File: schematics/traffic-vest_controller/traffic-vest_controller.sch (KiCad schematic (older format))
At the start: 21 parts

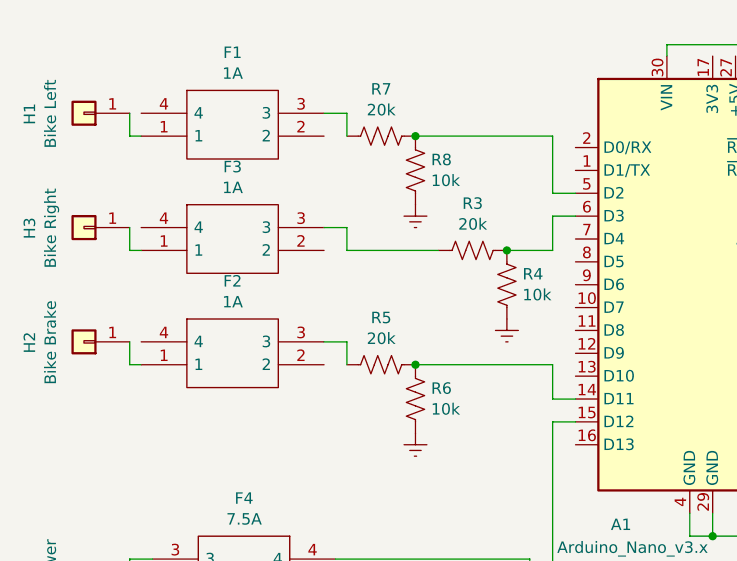
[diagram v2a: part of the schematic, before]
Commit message: Flipped nano, rearranged digital pin connecctions, futzed with connection spacing, re-routed tracks
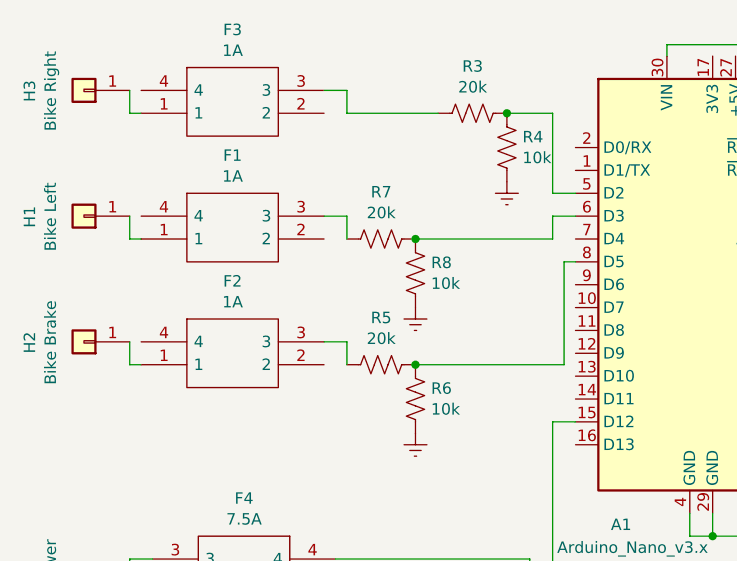
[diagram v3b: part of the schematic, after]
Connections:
- net at R5.1, R6.1: now also A1.8 (D5); no longer A1.14 (D11)
- net at R7.1, R8.1: now also A1.6 (D3); no longer A1.5 (D2)
- net at R3.1, R4.1: now also A1.5 (D2); no longer A1.6 (D3)
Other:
- moved on the sheet: F1, F3, H1, H3, R3, R4, R7, R8
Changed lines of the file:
@@
 L power:GNDREF #PWR0107
 U 1 1 62145970
-P 5400 3050
-F 0 "#PWR0107" H 5400 2800 50  0001 C CNN
-F 1 "GNDREF" H 5405 2877 50  0001 C CNN
-F 2 "" H 5400 3050 50  0001 C CNN
-F 3 "" H 5400 3050 50  0001 C CNN
-	1    5400 3050
+P 5400 2450
+F 0 "#PWR0107" H 5400 2200 50  0001 C CNN
+F 1 "GNDREF" H 5405 2277 50  0001 C CNN
+F 2 "" H 5400 2450 50  0001 C CNN
+F 3 "" H 5400 2450 50  0001 C CNN
+	1    5400 2450
 	1    0    0    -1
 $EndComp
@@
 L Device:R_US R3
 U 1 1 620FD795
-P 5250 2750
-F 0 "R3" V 5045 2750 50  0000 C CNN
-F 1 "20k" V 5136 2750 50  0000 C CNN
-F 2 "Resistor_THT:R_Axial_DIN0204_L3.6mm_D1.6mm_P5.08mm_Horizontal" V 5290 2740 50  0001 C CNN
-F 3 "~" H 5250 2750 50  0001 C CNN
-	1    5250 2750
+P 5250 2150
+F 0 "R3" V 5045 2150 50  0000 C CNN
+F 1 "20k" V 5136 2150 50  0000 C CNN
+F 2 "Resistor_THT:R_Axial_DIN0204_L3.6mm_D1.6mm_P5.08mm_Horizontal" V 5290 2140 50  0001 C CNN
+F 3 "~" H 5250 2150 50  0001 C CNN
+	1    5250 2150
 	0    1    1    0
 $EndComp
@@
 L Device:R_US R4
 U 1 1 620FBD59
-P 5400 2900
-F 0 "R4" H 5468 2946 50  0000 L CNN
-F 1 "10k" H 5468 2855 50  0000 L CNN
-F 2 "Resistor_THT:R_Axial_DIN0204_L3.6mm_D1.6mm_P5.08mm_Horizontal" V 5440 2890 50  0001 C CNN
-F 3 "~" H 5400 2900 50  0001 C CNN
-	1    5400 2900
+P 5400 2300
+F 0 "R4" H 5468 2346 50  0000 L CNN
+F 1 "10k" H 5468 2255 50  0000 L CNN
+F 2 "Resistor_THT:R_Axial_DIN0204_L3.6mm_D1.6mm_P5.08mm_Horizontal" V 5440 2290 50  0001 C CNN
+F 3 "~" H 5400 2300 50  0001 C CNN
+	1    5400 2300
 	1    0    0    -1
 $EndComp
@@
 L power:GNDREF #PWR0108
 U 1 1 62143F63
-P 5000 2550
-F 0 "#PWR0108" H 5000 2300 50  0001 C CNN
-F 1 "GNDREF" H 5005 2377 50  0001 C CNN
-F 2 "" H 5000 2550 50  0001 C CNN
-F 3 "" H 5000 2550 50  0001 C CNN
-	1    5000 2550
+P 5000 3000
+F 0 "#PWR0108" H 5000 2750 50  0001 C CNN
+F 1 "GNDREF" H 5005 2827 50  0001 C CNN
+F 2 "" H 5000 3000 50  0001 C CNN
+F 3 "" H 5000 3000 50  0001 C CNN
+	1    5000 3000
 	1    0    0    -1
 $EndComp
@@
 L Device:R_US R7
 U 1 1 620FC6E1
-P 4850 2250
-F 0 "R7" V 4645 2250 50  0000 C CNN
-F 1 "20k" V 4736 2250 50  0000 C CNN
-F 2 "Resistor_THT:R_Axial_DIN0204_L3.6mm_D1.6mm_P5.08mm_Horizontal" V 4890 2240 50  0001 C CNN
-F 3 "~" H 4850 2250 50  0001 C CNN
-	1    4850 2250
+P 4850 2700
+F 0 "R7" V 4645 2700 50  0000 C CNN
+F 1 "20k" V 4736 2700 50  0000 C CNN
+F 2 "Resistor_THT:R_Axial_DIN0204_L3.6mm_D1.6mm_P5.08mm_Horizontal" V 4890 2690 50  0001 C CNN
+F 3 "~" H 4850 2700 50  0001 C CNN
+	1    4850 2700
 	0    1    1    0
 $EndComp
@@
 L Device:R_US R8
 U 1 1 620FA2CA
-P 5000 2400
-F 0 "R8" H 5068 2446 50  0000 L CNN
-F 1 "10k" H 5068 2355 50  0000 L CNN
-F 2 "Resistor_THT:R_Axial_DIN0204_L3.6mm_D1.6mm_P5.08mm_Horizontal" V 5040 2390 50  0001 C CNN
-F 3 "~" H 5000 2400 50  0001 C CNN
-	1    5000 2400
-	1    0    0    -1
-$EndComp
-Wire Wire Line
-	5600 2500 5700 2500
-Connection ~ 5000 2250
+P 5000 2850
+F 0 "R8" H 5068 2896 50  0000 L CNN
+F 1 "10k" H 5068 2805 50  0000 L CNN
+F 2 "Resistor_THT:R_Axial_DIN0204_L3.6mm_D1.6mm_P5.08mm_Horizontal" V 5040 2840 50  0001 C CNN
+F 3 "~" H 5000 2850 50  0001 C CNN
+	1    5000 2850
+	1    0    0    -1
+$EndComp
+Connection ~ 5000 2700
 $Comp
 L Device:R_US R1
@@
 L traffic-vest_controller-rescue:3549-2-3549-2 F3
 U 1 1 622880EB
-P 3800 2650
-F 0 "F3" H 4200 2915 50  0000 C CNN
-F 1 "1A" H 4200 2824 50  0000 C CNN
-F 2 "3549-2:35492" H 4450 2750 50  0001 L CNN
-F 3 "https://componentsearchengine.com/Datasheets/1/3549-2.pdf" H 4450 2650 50  0001 L CNN
-F 4 "Fuse Holder FUSE SOCKET MINI HORZ .700 X .394" H 4450 2550 50  0001 L CNN "Description"
-F 5 "5.66" H 4450 2450 50  0001 L CNN "Height"
-F 6 "534-3549-2" H 4450 2350 50  0001 L CNN "Mouser Part Number"
-F 7 "https://www.mouser.co.uk/ProductDetail/Keystone-Electronics/3549-2?qs=fP5bVVCrK%2Fei3gwwxH1JKw%3D%3D" H 4450 2250 50  0001 L CNN "Mouser Price/Stock"
-F 8 "Keystone Electronics" H 4450 2150 50  0001 L CNN "Manufacturer_Name"
-F 9 "3549-2" H 4450 2050 50  0001 L CNN "Manufacturer_Part_Number"
-	1    3800 2650
+P 3800 2050
+F 0 "F3" H 4200 2315 50  0000 C CNN
+F 1 "1A" H 4200 2224 50  0000 C CNN
+F 2 "3549-2:35492" H 4450 2150 50  0001 L CNN
+F 3 "https://componentsearchengine.com/Datasheets/1/3549-2.pdf" H 4450 2050 50  0001 L CNN
+F 4 "Fuse Holder FUSE SOCKET MINI HORZ .700 X .394" H 4450 1950 50  0001 L CNN "Description"
+F 5 "5.66" H 4450 1850 50  0001 L CNN "Height"
+F 6 "534-3549-2" H 4450 1750 50  0001 L CNN "Mouser Part Number"
+F 7 "https://www.mouser.co.uk/ProductDetail/Keystone-Electronics/3549-2?qs=fP5bVVCrK%2Fei3gwwxH1JKw%3D%3D" H 4450 1650 50  0001 L CNN "Mouser Price/Stock"
+F 8 "Keystone Electronics" H 4450 1550 50  0001 L CNN "Manufacturer_Name"
+F 9 "3549-2" H 4450 1450 50  0001 L CNN "Manufacturer_Part_Number"
+	1    3800 2050
 	1    0    0    -1
 $EndComp
@@
 L Connector_Generic:Conn_01x01 H1
 U 1 1 622B1C15
-P 3550 2150
-F 0 "H1" V 3787 2153 50  0000 C CNN
-F 1 "Bike Left" V 3696 2153 50  0000 C CNN
-F 2 "Connector_Wire:SolderWirePad_1x01_Drill1.5mm" H 3550 2150 50  0001 C CNN
-F 3 "~" H 3550 2150 50  0001 C CNN
-	1    3550 2150
+P 3550 2600
+F 0 "H1" V 3787 2603 50  0000 C CNN
+F 1 "Bike Left" V 3696 2603 50  0000 C CNN
+F 2 "Connector_Wire:SolderWirePad_1x01_Drill1.5mm" H 3550 2600 50  0001 C CNN
+F 3 "~" H 3550 2600 50  0001 C CNN
+	1    3550 2600
 	-1   0    0    1
 $EndComp
@@
 L Connector_Generic:Conn_01x01 H3
 U 1 1 622B1527
-P 3550 2650
-F 0 "H3" V 3787 2653 50  0000 C CNN
-F 1 "Bike Right" V 3696 2653 50  0000 C CNN
-F 2 "Connector_Wire:SolderWirePad_1x01_Drill1.5mm" H 3550 2650 50  0001 C CNN
-F 3 "~" H 3550 2650 50  0001 C CNN
-	1    3550 2650
+P 3550 2050
+F 0 "H3" V 3787 2053 50  0000 C CNN
+F 1 "Bike Right" V 3696 2053 50  0000 C CNN
+F 2 "Connector_Wire:SolderWirePad_1x01_Drill1.5mm" H 3550 2050 50  0001 C CNN
+F 3 "~" H 3550 2050 50  0001 C CNN
+	1    3550 2050
 	-1   0    0    1
 $EndComp
@@
 Wire Wire Line
 	5600 3500 5600 4450
-Wire Wire Line
-	5600 2250 5600 2500
-Connection ~ 5400 2750
+Connection ~ 5400 2150
 $Comp
 L traffic-vest_controller-rescue:3549-2-3549-2 F4
@@
 $EndComp
 Wire Wire Line
-	5600 2750 5600 2600
-Wire Wire Line
-	5600 2600 5700 2600
-Wire Wire Line
-	5400 2750 5600 2750
-Wire Wire Line
-	5600 3250 5600 3400
-Wire Wire Line
-	5600 3400 5700 3400
+	5400 2150 5600 2150
 $Comp
 L traffic-vest_controller-rescue:3549-2-3549-2 F2
@@
 	1    0    0    -1
 $EndComp
-Wire Wire Line
-	5000 3250 5600 3250
 Connection ~ 5000 3250
 Wire Wire Line
@@
 	5600 4450 6850 4450
 Wire Wire Line
-	3750 2650 3750 2750
-Wire Wire Line
-	3750 2750 3800 2750
-Wire Wire Line
-	4600 2650 4700 2650
-Wire Wire Line
-	4700 2650 4700 2750
-Wire Wire Line
-	4700 2750 5100 2750
+	3750 2050 3750 2150
+Wire Wire Line
+	3750 2150 3800 2150
+Wire Wire Line
+	4600 2050 4700 2050
+Wire Wire Line
+	4700 2050 4700 2150
+Wire Wire Line
+	4700 2150 5100 2150
 Wire Wire Line
 	3750 3150 3750 3250
@@
 L traffic-vest_controller-rescue:3549-2-3549-2 F1
 U 1 1 62286CF1
-P 3800 2150
-F 0 "F1" H 4200 2415 50  0000 C CNN
-F 1 "1A" H 4200 2324 50  0000 C CNN
-F 2 "3549-2:35492" H 4450 2250 50  0001 L CNN
-F 3 "https://componentsearchengine.com/Datasheets/1/3549-2.pdf" H 4450 2150 50  0001 L CNN
-F 4 "Fuse Holder FUSE SOCKET MINI HORZ .700 X .394" H 4450 2050 50  0001 L CNN "Description"
-F 5 "5.66" H 4450 1950 50  0001 L CNN "Height"
-F 6 "534-3549-2" H 4450 1850 50  0001 L CNN "Mouser Part Number"
-F 7 "https://www.mouser.co.uk/ProductDetail/Keystone-Electronics/3549-2?qs=fP5bVVCrK%2Fei3gwwxH1JKw%3D%3D" H 4450 1750 50  0001 L CNN "Mouser Price/Stock"
-F 8 "Keystone Electronics" H 4450 1650 50  0001 L CNN "Manufacturer_Name"
-F 9 "3549-2" H 4450 1550 50  0001 L CNN "Manufacturer_Part_Number"
-	1    3800 2150
-	1    0    0    -1
-$EndComp
-Wire Wire Line
-	5000 2250 5600 2250
-Wire Wire Line
-	4600 2150 4700 2150
-Wire Wire Line
-	4700 2150 4700 2250
-Wire Wire Line
-	3750 2150 3750 2250
-Wire Wire Line
-	3750 2250 3800 2250
+P 3800 2600
+F 0 "F1" H 4200 2865 50  0000 C CNN
+F 1 "1A" H 4200 2774 50  0000 C CNN
+F 2 "3549-2:35492" H 4450 2700 50  0001 L CNN
+F 3 "https://componentsearchengine.com/Datasheets/1/3549-2.pdf" H 4450 2600 50  0001 L CNN
+F 4 "Fuse Holder FUSE SOCKET MINI HORZ .700 X .394" H 4450 2500 50  0001 L CNN "Description"
+F 5 "5.66" H 4450 2400 50  0001 L CNN "Height"
+F 6 "534-3549-2" H 4450 2300 50  0001 L CNN "Mouser Part Number"
+F 7 "https://www.mouser.co.uk/ProductDetail/Keystone-Electronics/3549-2?qs=fP5bVVCrK%2Fei3gwwxH1JKw%3D%3D" H 4450 2200 50  0001 L CNN "Mouser Price/Stock"
+F 8 "Keystone Electronics" H 4450 2100 50  0001 L CNN "Manufacturer_Name"
+F 9 "3549-2" H 4450 2000 50  0001 L CNN "Manufacturer_Part_Number"
+	1    3800 2600
+	1    0    0    -1
+$EndComp
+Wire Wire Line
+	5000 2700 5600 2700
+Wire Wire Line
+	4600 2600 4700 2600
+Wire Wire Line
+	4700 2600 4700 2700
+Wire Wire Line
+	3750 2600 3750 2700
+Wire Wire Line
+	3750 2700 3800 2700
 Wire Wire Line
 	4600 3150 4700 3150
 Wire Wire Line
 	4700 3150 4700 3250
+Wire Wire Line
+	5650 3250 5650 2800
+Wire Wire Line
+	5650 2800 5700 2800
+Wire Wire Line
+	5000 3250 5650 3250
+Wire Wire Line
+	5600 2700 5600 2600
+Wire Wire Line
+	5600 2600 5700 2600
+Wire Wire Line
+	5600 2150 5600 2500
+Wire Wire Line
+	5600 2500 5700 2500
 $EndSCHEMATC

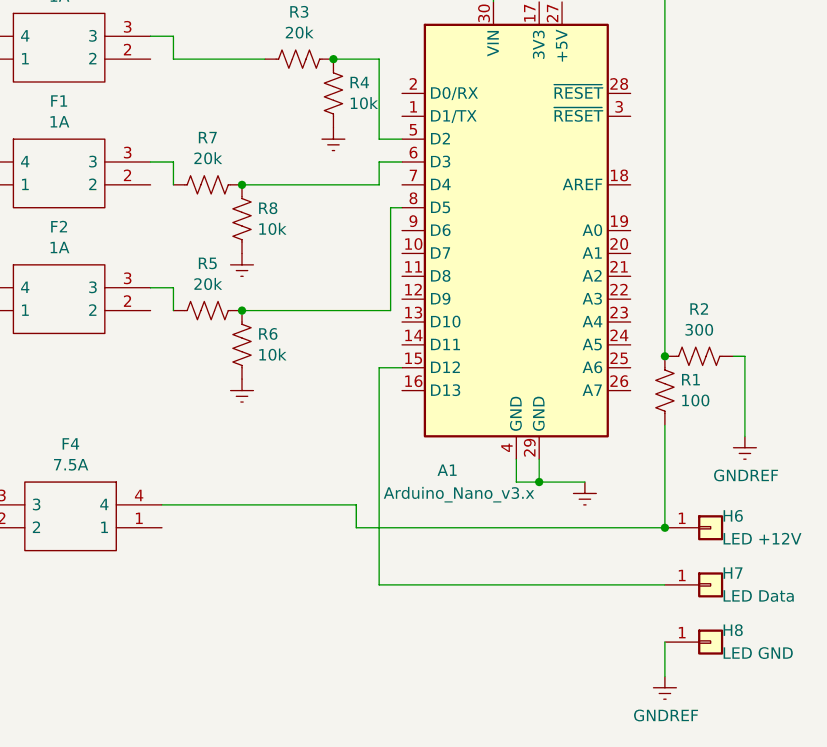
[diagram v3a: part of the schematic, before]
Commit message: Fixed ground pour to make contiguous zone.  One more rearrangement of circuits to pins for cleanliness and short tracks.  Generated gerbers and drill file for cutting.
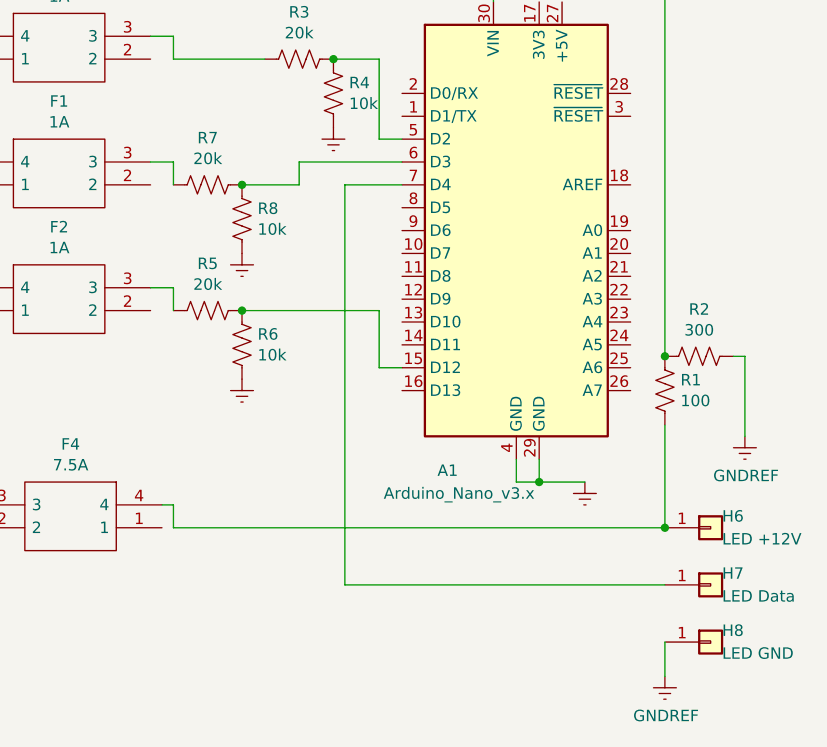
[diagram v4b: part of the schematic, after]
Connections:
- net at A1.15 (D12): now also R5.1, R6.1; no longer H7.1 (Pin_1)
- net at A1.7 (D4): now also H7.1 (Pin_1)
- now unconnected: A1.8 (D5)
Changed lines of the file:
@@
 	1    0    0    -1
 $EndComp
-Connection ~ 5000 2700
 $Comp
 L Device:R_US R1
@@
 Wire Wire Line
 	6300 4000 6500 4000
-Wire Wire Line
-	5700 3500 5600 3500
 $Comp
 L traffic-vest_controller-rescue:3549-2-3549-2 F3
@@
 Wire Wire Line
 	6850 4700 6850 4850
-Wire Wire Line
-	5600 3500 5600 4450
 Connection ~ 5400 2150
 $Comp
@@
 	1    0    0    -1
 $EndComp
-Connection ~ 5000 3250
 Wire Wire Line
 	6850 3750 6850 4200
@@
 	3750 4700 3750 4850
 Wire Wire Line
-	5600 4450 6850 4450
-Wire Wire Line
 	3750 2050 3750 2150
 Wire Wire Line
@@
 Wire Wire Line
 	3750 3250 3800 3250
-Wire Wire Line
-	5500 4100 5500 4200
-Wire Wire Line
-	5500 4200 6850 4200
 Connection ~ 6850 4200
 Wire Wire Line
@@
 Wire Wire Line
 	3750 4100 3850 4100
-Wire Wire Line
-	4650 4100 5500 4100
 $Comp
 L traffic-vest_controller-rescue:3549-2-3549-2 F1
@@
 $EndComp
 Wire Wire Line
-	5000 2700 5600 2700
-Wire Wire Line
 	4600 2600 4700 2600
 Wire Wire Line
@@
 	4700 3150 4700 3250
 Wire Wire Line
-	5650 3250 5650 2800
-Wire Wire Line
-	5650 2800 5700 2800
-Wire Wire Line
-	5000 3250 5650 3250
-Wire Wire Line
-	5600 2700 5600 2600
-Wire Wire Line
-	5600 2600 5700 2600
-Wire Wire Line
 	5600 2150 5600 2500
 Wire Wire Line
 	5600 2500 5700 2500
+Wire Wire Line
+	5250 2600 5250 2700
+Wire Wire Line
+	5250 2700 5000 2700
+Wire Wire Line
+	5250 2600 5700 2600
+Connection ~ 5000 2700
+Wire Wire Line
+	4700 4200 4700 4100
+Wire Wire Line
+	4700 4100 4650 4100
+Wire Wire Line
+	4700 4200 6850 4200
+Wire Wire Line
+	5600 3500 5600 3250
+Wire Wire Line
+	5600 3250 5000 3250
+Wire Wire Line
+	5600 3500 5700 3500
+Connection ~ 5000 3250
+Wire Wire Line
+	5700 2700 5450 2700
+Wire Wire Line
+	5450 2700 5450 4450
+Wire Wire Line
+	5450 4450 6850 4450
 $EndSCHEMATC

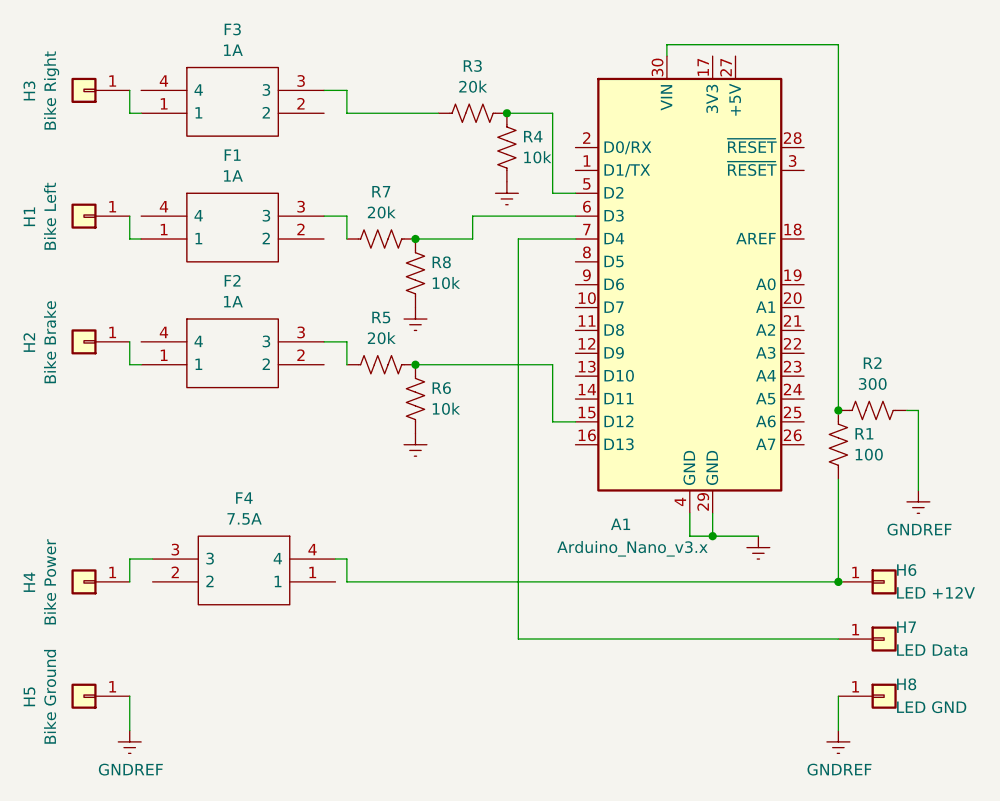
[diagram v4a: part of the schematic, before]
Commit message: Board V3, child of V1: \n* Corrected orientation of nano\n* Re-ran tracks\n* Incorporated V2 improvements: wire drill hole sizes, extra spacing between mount and relief holes, name and course etched into copper
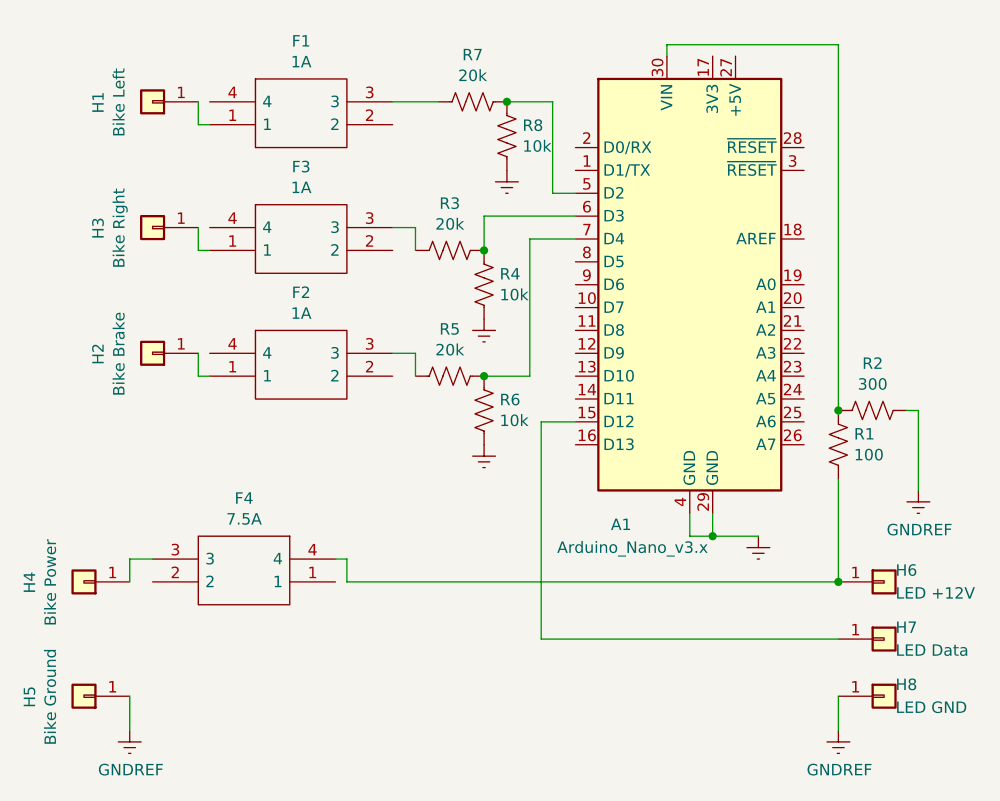
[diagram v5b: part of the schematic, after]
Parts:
- H1, H2, H3, H4, H5: footprint Connector_Wire:SolderWirePad_1x01_Drill1.5mm -> Connector_Wire:SolderWirePad_1x01_Drill2mm
- R1, R2, R3, R4, R5, R6, R7, R8: footprint Resistor_THT:R_Axial_DIN0204_L3.6mm_D1.6mm_P5.08mm_Horizontal -> Resistor_THT:R_Axial_DIN0207_L6.3mm_D2.5mm_P7.62mm_Horizontal
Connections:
- net at R5.1, R6.1: now also A1.7 (D4); no longer A1.15 (D12)
- net at R3.1, R4.1: now also A1.6 (D3); no longer A1.5 (D2)
- net at R7.1, R8.1: now also A1.5 (D2); no longer A1.6 (D3)
- net at H7.1 (Pin_1): now also A1.15 (D12); no longer A1.7 (D4)
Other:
- moved on the sheet: F1, F2, F3, H1, H2, H3, R3, R4, R5, R6, R7, R8
